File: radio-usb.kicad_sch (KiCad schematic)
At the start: 229 parts, among them J1 Barrel_Jack, J10 Conn_Coaxial, J11 ACJS-MHDRM, J12 ACJS-MHDRM, J2 miniUSB, J3 15EDGRC-3.5-03P-14, J4 DB9_Female, J5 EEP_EN, J6 Mini-DIN-6, J7 EDAC 690-008-221-904, J8 DB9_Male, J9 Conn_Coaxial, Q1 BC846C, Q2 BC846, Q3 BC846, Q4 BC846, Q5 BC856, SW1 SW_Push_DPDT, SW2 SW_SPDT, SW3 SW_SPDT, SW4 SW_DIP_x04, SW5 SW_DIP_x04, SW6 SW_DPDT_x2, SW7 SW_SPDT, U1 L7805, U10 AP2171W, U11 TLP2662, U12 TLP2662, U13 MAX3232, U14 93CxxC, U15 PCM2902, U17 FT2232HL, U18 PC817, U19 CRIYCHLEY9000, U2 24LC04, U20 PC817, U21 PC817, U22 CRIYCHLEY9000, U23 LMV321IDBVR, U3 APX809_810-xxSA, U4 AP22814AW5, U5 AP22814AW5, U6 USB2514B_Bi, U7 LM1117-3.3, U8 TBA 1-0511, U9 4069, X1 MAB5SH, Y1 24MHz, Y2 12MHz, Y3 12M

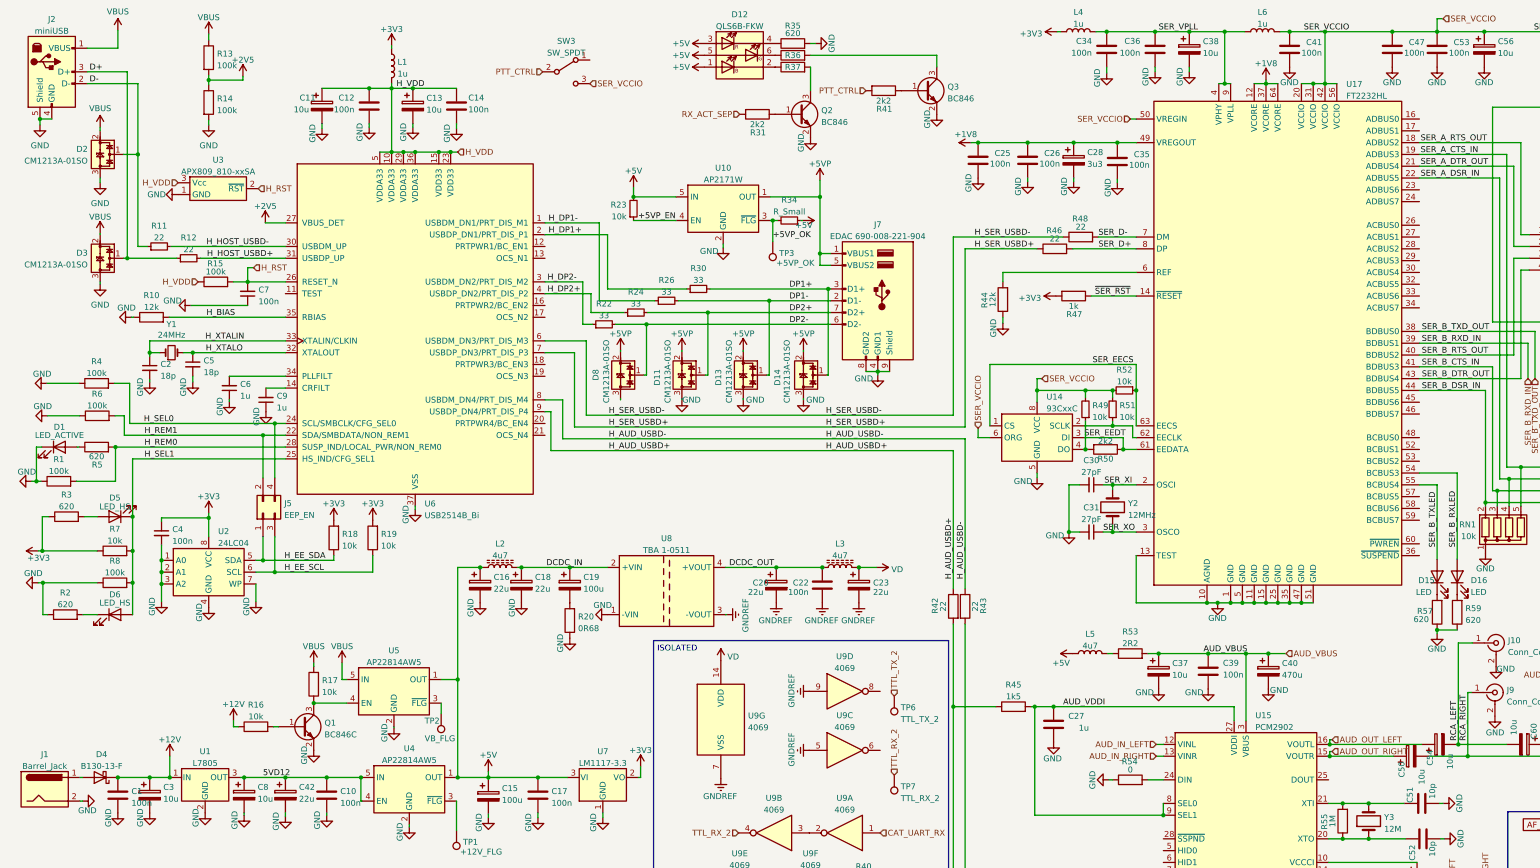
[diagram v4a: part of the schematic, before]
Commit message: everything routed, bourns audio transformer footprint correcred, ground polygons
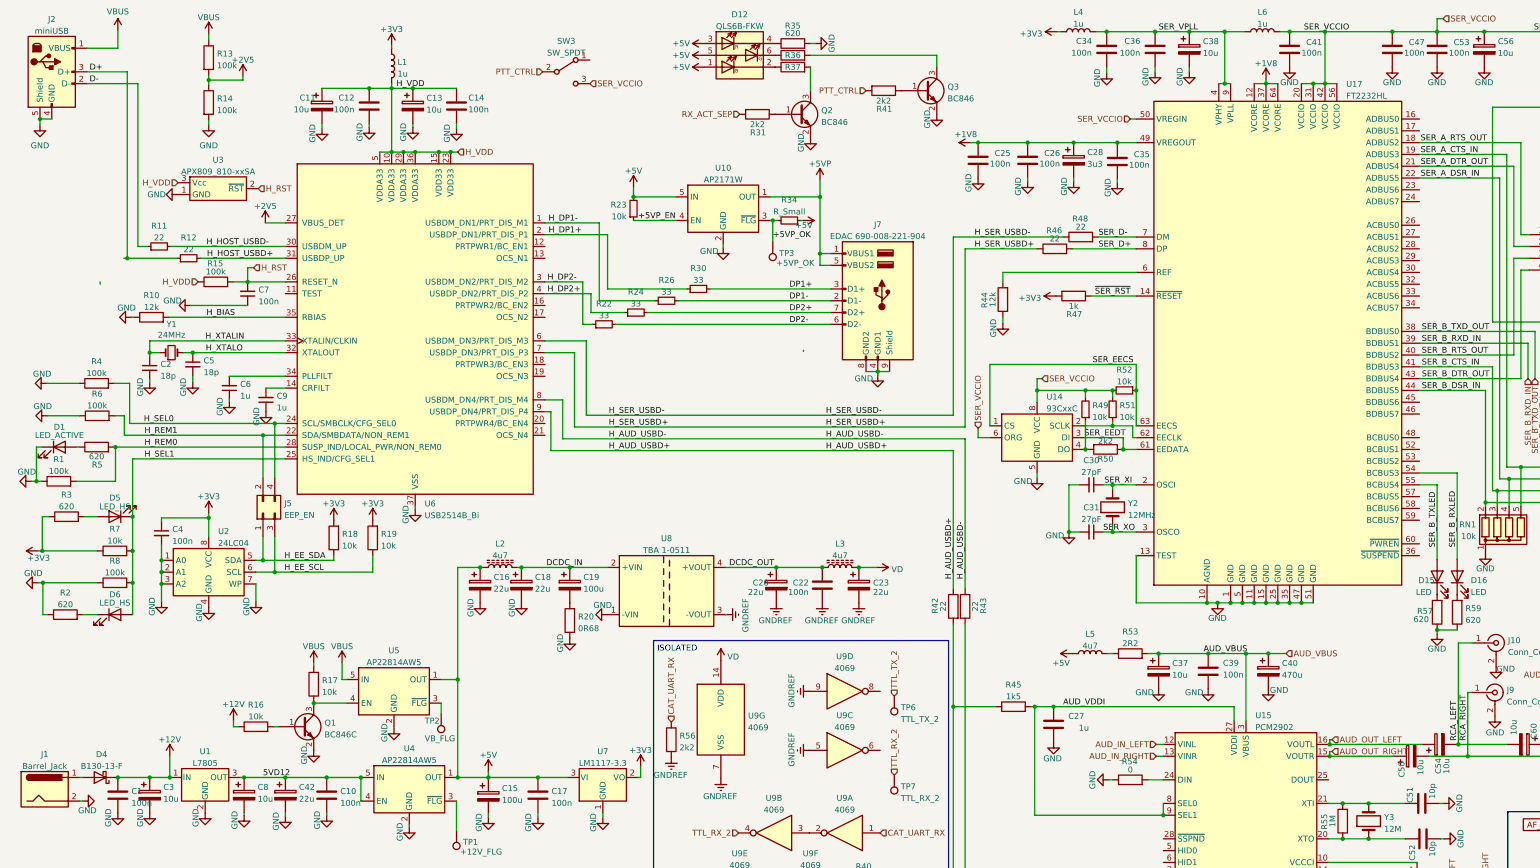
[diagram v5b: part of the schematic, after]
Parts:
- removed D11, D13, D14, D2, D3, D8: CM1213A-01SO, Package_TO_SOT_SMD:SOT-23, symbol Power_Protection:CM1213A-01SO
- added R56: 2k2, Resistor_SMD:R_0805_2012Metric_Pad1.20x1.40mm_HandSolder, symbol Device:R
- TP1, TP2, TP4, TP5, TP6, TP9: footprint TestPoint:TestPoint_Pad_D2.0mm -> TestPoint:TestPoint_Pad_D1.0mm
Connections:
- net CAT_UART_RX: now also R56.1
- net GNDREF: now also R56.2

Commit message: silkscreen description and test points
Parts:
- added TP10: AUD_OUT_L, TestPoint:TestPoint_Pad_D2.0mm, symbol Connector:TestPoint
- added TP11: AUD_OUT_R, TestPoint:TestPoint_Pad_D2.0mm, symbol Connector:TestPoint
- added TP12: OPAMP_BIAS, TestPoint:TestPoint_Pad_D2.0mm, symbol Connector:TestPoint
- added TP13: PTT_CTRL, TestPoint:TestPoint_Pad_D2.0mm, symbol Connector:TestPoint
- added TP14: USB_GROUND, TestPoint:TestPoint_Pad_D2.0mm, symbol Connector:TestPoint
- added TP15: GROUND, TestPoint:TestPoint_Pad_D2.0mm, symbol Connector:TestPoint
- added TP16: +12V, TestPoint:TestPoint_Pad_D2.0mm, symbol Connector:TestPoint
- added TP17: +2V5, TestPoint:TestPoint_Pad_D2.0mm, symbol Connector:TestPoint
- added TP18: +5V, TestPoint:TestPoint_Pad_D2.0mm, symbol Connector:TestPoint
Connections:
- net +12V: now also TP16.1
- net +2V5: now also TP17.1
- net +5V: now also TP18.1
- net AUD_OUT_LEFT: now also TP10.1
- net AUD_OUT_RIGHT: now also TP11.1
- net GND: now also TP14.1
- net GNDREF: now also TP15.1
- net PTT_CTRL: now also TP13.1
- net at R64.1, R71.2, R72.2: now also TP12.1

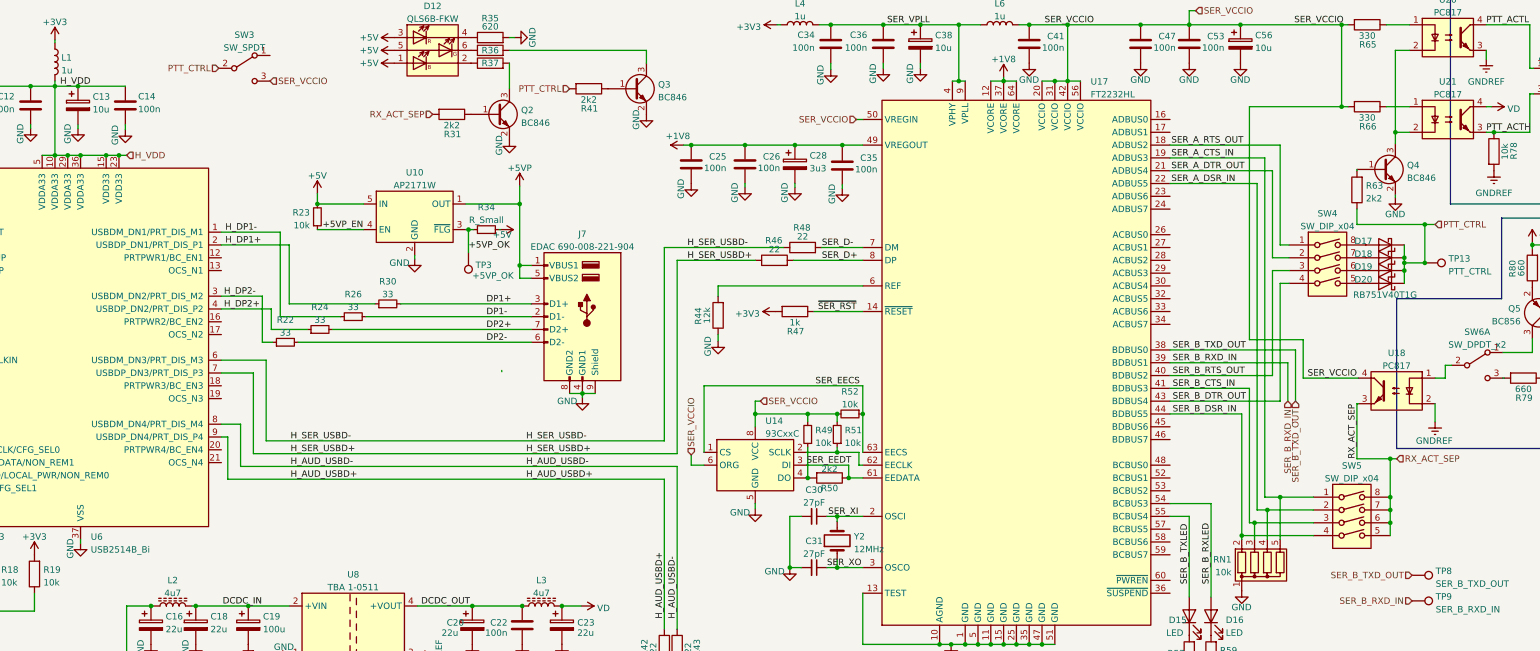
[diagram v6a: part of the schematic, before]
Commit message: fixed mini din 6 orientation, fix via size problems
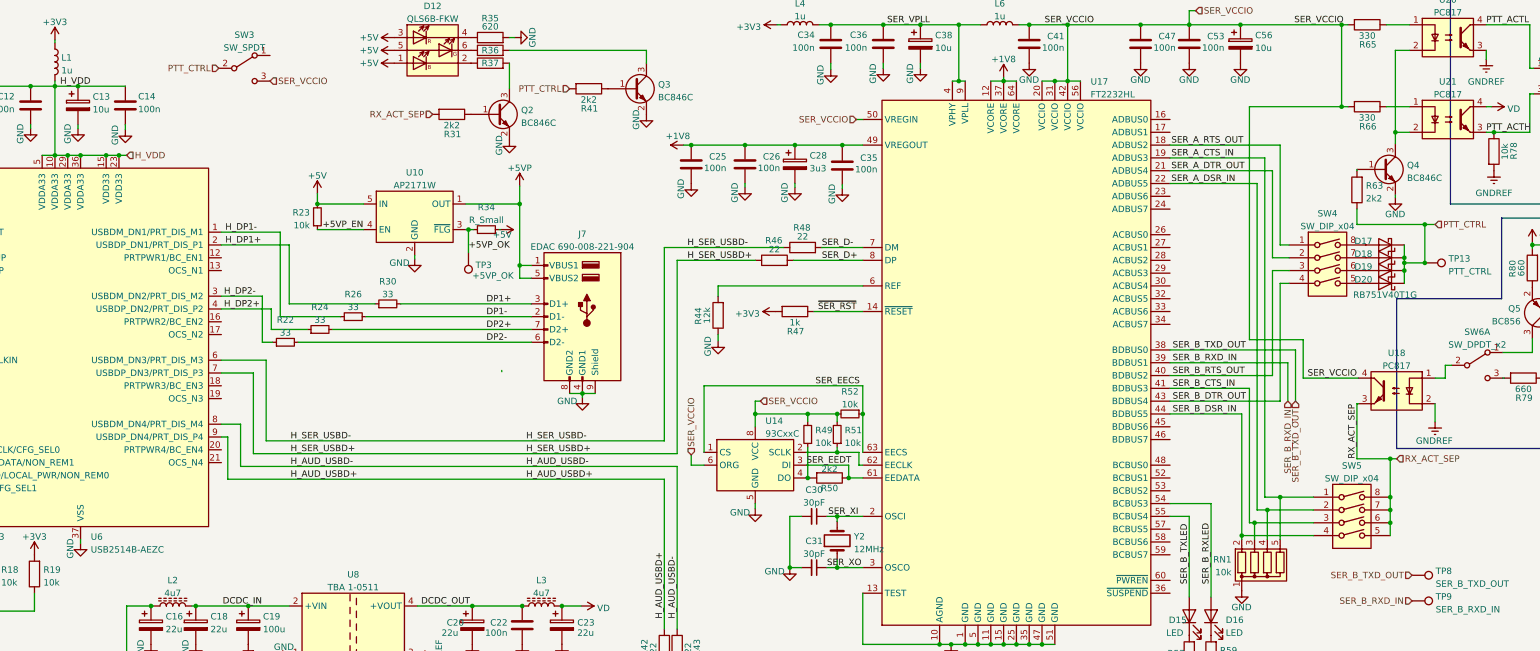
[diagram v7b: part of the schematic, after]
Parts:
- C1, C10, C12, C14, C17, C21, C22, C25, C26, C34, C35, C36, C39, C4, C41, C47, C53, C7: DESCRIPTION (none) -> 08051C104KAT2A KYOCERA AVX
- C2, C5: DESCRIPTION (none) -> 08055A180JAT2A KYOCERA AVX
- C24, C29, C32, C33: DESCRIPTION (none) -> 06033G104ZAT2A KYOCERA AVX
- C27, C43, C45, C46, C6, C9: DESCRIPTION (none) -> 0805YC105KAT2A KYOCERA AVX
- C28: DESCRIPTION (none) -> 0805ZD335KAT2A KYOCERA AVX
- C30, C31: value 27pF -> 30pF; DESCRIPTION (none) -> 08055A300JAT2A KYOCERA AVX
- C51, C52: DESCRIPTION (none) -> 08055A100JAT2A KYOCERA AVX
- C55, C57: DESCRIPTION (none) -> 08051C223KAT2A KYOCERA AVX
- C58, C59: DESCRIPTION (none) -> 0805YC475KAT2A KYOCERA AVX
- D1: DESCRIPTION (none) -> KPT-2012CGCK KINGBRIGHT ELECTRONIC
- D10, D17, D18, D19, D20, D9: DESCRIPTION (none) -> RB751V40T1G ONSEMI
- D12: DESCRIPTION (none) -> 1882.2781 MENTOR
- D15, D16: DESCRIPTION (none) -> KP-2012SYCK KINGBRIGHT ELECTRONIC
- D4: DESCRIPTION (none) -> B130-13-F DIODES INCORPORATED
- D5, D6: DESCRIPTION (none) -> KPT-2012SURC KINGBRIGHT ELECTRONIC
- D7: DESCRIPTION (none) -> 1N4148W-AQ DIOTEC SEMICONDUCTOR
- J11, J12: DESCRIPTION (none) -> ACJS-MHDRM AMPHENOL
- J2: DESCRIPTION (none) -> DS1099-WN0 CONNFLY
- J4: DESCRIPTION (none) -> DE09-SN-24 ADAM TECH
- J6: DESCRIPTION (none) -> 4850.2610 SCHURTER
- J7: DESCRIPTION (none) -> EDAC 690-008-221-904
- J8: DESCRIPTION (none) -> DE09-PN-24 ADAM TECH
- L1, L4, L6: footprint Inductor_SMD:L_1210_3225Metric_Pad1.42x2.65mm_HandSolder -> Inductor_SMD:L_0805_2012Metric_Pad1.15x1.40mm_HandSolder; DESCRIPTION (none) -> Viking NL05KTC1R0
- Q1: DESCRIPTION (none) -> BC846C-AQ DIOTEC SEMICONDUCTOR
- Q2, Q3, Q4: value BC846 -> BC846C; DESCRIPTION (none) -> BC846C-AQ DIOTEC SEMICONDUCTOR
- Q5: DESCRIPTION (none) -> BC856B-AQ DIOTEC SEMICONDUCTOR
- U10: DESCRIPTION (none) -> DIODES INCORPORATED AP2171WG-7
- U17: DESCRIPTION (none) -> FTDI FT2232HL
- U4, U5: DESCRIPTION (none) -> DIODES INCORPORATED AP22814AW5-7
- U6: value USB2514B_Bi -> USB2514B-AEZC; DESCRIPTION (none) -> MICROCHIP TECHNOLOGY USB2514B-AEZC

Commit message: gerber files and another fabrication output
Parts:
- C30, C31: value 30pF -> 18p; DESCRIPTION 08055A300JAT2A KYOCERA AVX -> 08055A180FAT2A KYOCERA AVX
- C51, C52: value 10p -> 18p; DESCRIPTION 08055A100JAT2A KYOCERA AVX -> 08055A180FAT2A KYOCERA AVX
- R1, R13, R14, R15, R16, R18, R19, R21, R23, R38, R39, R4, R49, R51, R52, R6, R61, R62, R64, R67, R68, R7, R71, R72, R77, R8: DESCRIPTION (none) -> ERJ6ENF1002V PANASONIC
- R10, R44: DESCRIPTION (none) -> ERJ6ENF1202V PANASONIC
- R11, R12, R42, R43, R46, R48: DESCRIPTION (none) -> ERJ3EKF22R0V PANASONIC
- R17, R78: DESCRIPTION (none) -> ERJ3EKF1002V PANASONIC
- R2, R3, R5, R57, R59: DESCRIPTION (none) -> ERJ6GEYJ621V PANASONIC
- R22, R24, R26, R30: DESCRIPTION (none) -> ERJ3EKF33R0V PANASONIC
- R25, R29, R31, R40, R41, R50, R56, R63: DESCRIPTION (none) -> ERJ6ENF2201V PANASONIC
- R27, R28, R32, R33, R79, R80: value 660 -> 680; DESCRIPTION (none) -> ERA6AEB681V PANASONIC
- R35, R36, R37: DESCRIPTION (none) -> ERJ3EKF6200V PANASONIC
- R45: DESCRIPTION (none) -> ERA6AEB152V PANASONIC
- R47: DESCRIPTION (none) -> ERJ6ENF1001V PANASONIC
- R53: DESCRIPTION (none) -> ERJP06J2R2V PANASONIC
- R54: DESCRIPTION (none) -> ERJ6GEY0R00V PANASONIC
- R55: DESCRIPTION (none) -> ERJ6ENF1004V PANASONIC
- R58, R60: DESCRIPTION (none) -> 0805S8F160JT5E ROYAL OHM
- R65, R66: DESCRIPTION (none) -> ERJ6ENF3300V PANASONIC
- R69: DESCRIPTION (none) -> ERJ3GEY0R00V PANASONIC
- R81: DESCRIPTION (none) -> ERJ6ENF2202V PANASONIC
- R9: DESCRIPTION (none) -> ERJ6ENF4701V PANASONIC
- RN1: DESCRIPTION (none) -> RNLA05G0103B0E ROYAL OHM
- SW4, SW5: DESCRIPTION (none) -> NIDEC CHS-04B
- U11, U12: DESCRIPTION (none) -> TLP2662F TOSHIBA
- U14: DESCRIPTION (none) -> 93C46A-I/P MICROCHIP TECHNOLOGY
- U15: value PCM2902 -> PCM2900CDB; DESCRIPTION (none) -> TEXAS INSTRUMENTS PCM2900CDB
- U2: DESCRIPTION (none) -> 24LC04BH-I/P MICROCHIP TECHNOLOGY
- U3: DESCRIPTION (none) -> APX809S-29SA-7 DIODES INCORPORATED
- U7: DESCRIPTION (none) -> LM1117DTX-3.3 TEXAS INSTRUMENTS
- Y2, Y3: DESCRIPTION (none) -> 7V-12.000MDDJ-T TXC
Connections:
- net SER_XI: now also Y2.1; no longer Y2.2
- net SER_XO: now also Y2.2; no longer Y2.1
